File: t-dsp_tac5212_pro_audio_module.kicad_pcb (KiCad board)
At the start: 4 copper layers, 42 x 26.5 mm, 110 parts, among them J3V108 jumper, J5V108 jumper, T108 Tab, T109 Tab, T110 Tab, T111 Tab, U108 Single Buffer with Tri-state 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, U109 3.3v LDO - TLV74133PDBVR

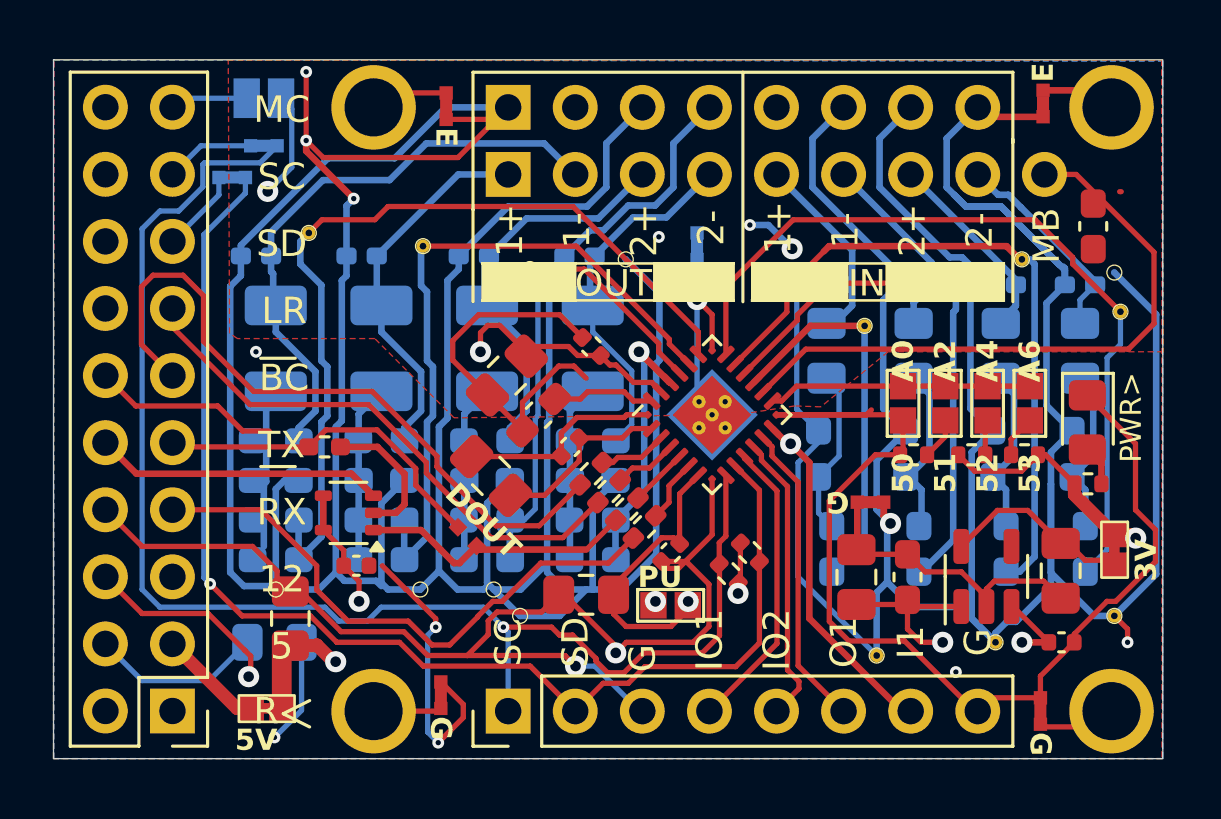
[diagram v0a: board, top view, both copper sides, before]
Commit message: Add 3D render gallery, update schematic for production
- Add interactive 3D render gallery with All Components / SMD Only tabs
- Add gallery.html page deployed to GitHub Pages alongside iBOM
- Update KiBot config: _th_ prefix file_ids, exclude_tht filter, 3d_renders_smd output
- Update CI workflow to deploy renders and gallery to GitHub Pages
- Update README with gallery thumbnail grid and links
- Schematic updates: 49.9Ω ADC input resistors, 100K bias pull-downs, component refinements
- Updated board outline footprint, schematic library, PCB layout, and 3D STEP models
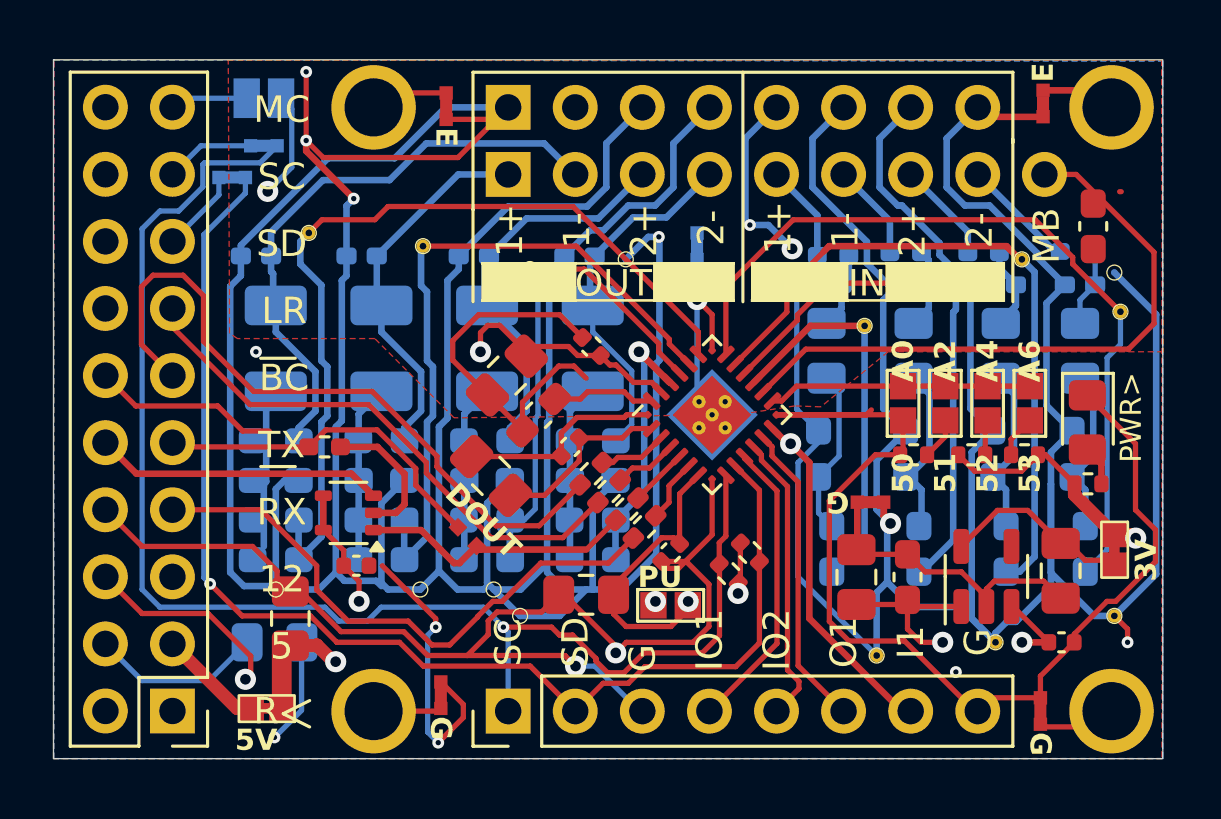
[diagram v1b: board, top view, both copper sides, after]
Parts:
- added R109: 49.9, project_fp:R_0402_1005Metric_Pad0.72x0.64mm_HandSolder, B.Cu at (120.0, 105.2)
- added R110: 49.9, project_fp:R_0402_1005Metric_Pad0.72x0.64mm_HandSolder, B.Cu at (123.5, 105.2)
- added R112: 49.9, project_fp:R_0402_1005Metric_Pad0.72x0.64mm_HandSolder, B.Cu at (117.1, 105.2)
- added R113: 49.9, project_fp:R_0402_1005Metric_Pad0.72x0.64mm_HandSolder, B.Cu at (114.3, 105.3)
- C124: value 10UF confirm polarity -> 10uF
- C125, C126, C127: value 10UF -> 10uF
- C131: footprint project_fp:C_0805_2012Metric_Pad1.15x1.40mm_HandSolder -> project_fp:C_0805_2012Metric_Pad1.18x1.45mm_HandSolder
- D108, D109, D110, D111, D112: value TPD1E10B06 -> TPD1E10B06DPYR
- D113, D114, D115: value TPD1E1B04 - 0402 size -> TPD1E10B06DPYR
- R117, R125: value 27 ohm -> 33 ohm
- TAC5212: value TAC5212 -> TAC5212IRGER
- renumbered R109 to R128, R131 to R129, R134 to R130, R136 to R134, R130 to R136, R126 to R140, R129 to R161, R116 to R162, R133 to R163
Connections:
- D112 pad 1: IN2M+ -> Net-(D112-K-Pad1)
- D113 pad 1: IN2P+ -> Net-(D113-K-Pad1)
- D114 pad 1: IN1M+ -> Net-(D114-K-Pad1)
- D115 pad 1: IN1P+ -> Net-(D115-K-Pad1)
- FB108 pad 1: IN2M+ -> Net-(D112-K-Pad1)
- FB109 pad 1: IN2P+ -> Net-(D113-K-Pad1)
- FB110 pad 1: IN1M+ -> Net-(D114-K-Pad1)
- FB111 pad 1: IN1P+ -> Net-(D115-K-Pad1)
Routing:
- net IN2P+: track 7.57 -> 3.86 mm
- net IN2M+: track 7.95 -> 4.33 mm
- net IN1M+: track 7.30 -> 3.69 mm
- net IN1P+: track 7.11 -> 3.70 mm
- net Net-(D113-K-Pad1): track 0.00 -> 3.21 mm
- net Net-(D114-K-Pad1): track 0.00 -> 3.03 mm
- net Net-(D112-K-Pad1): track 0.00 -> 3.01 mm
- net Net-(D115-K-Pad1): track 0.00 -> 2.93 mm
- net Earth: track 295.2 -> 296.4 mm

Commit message: Shrink board size to match Teensy audio adaptor shield dimensions
Update board outline width (42mm → 41.34mm), add connector 3D models
for pin sockets, and refresh PCB layout.
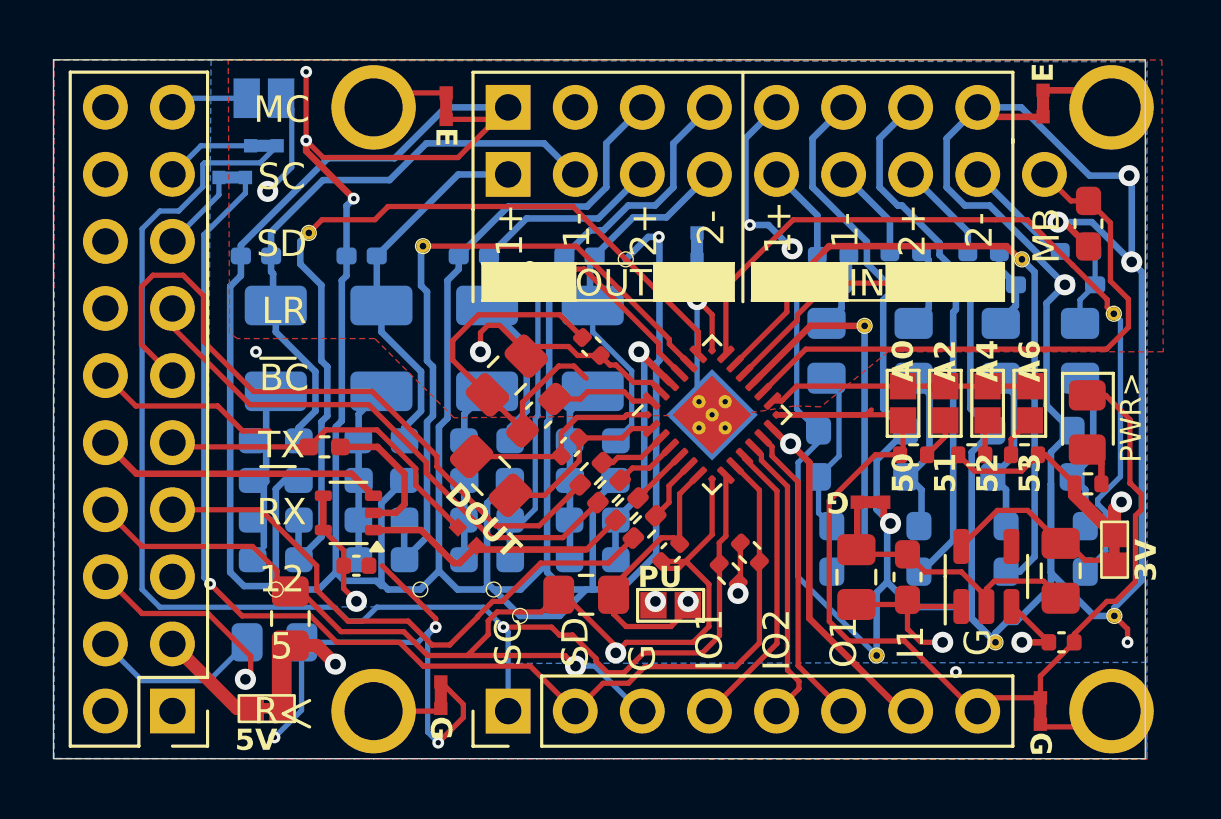
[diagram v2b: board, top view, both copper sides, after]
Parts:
- removed G108: VIA, project_fp:SMD_ROUTING_PAD
- moved T110 0.66 mm to (126.2, 103.9)
- moved T111 0.66 mm to (126.2, 118.4)
- moved INM2 0.26 mm to (125.0, 107.6)
- moved C118 0.21 mm to (124.0, 104.2)
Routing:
- net Earth: track 296.4 -> 311.3 mm, vias 9 -> 13
- net GNDD: track 170.1 -> 175.4 mm
- net MICBIAS: track 23.9 -> 22.3 mm
- added copper zone on B.Cu, net GNDD
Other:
- board size 42 x 26.5 mm -> 41.3 x 26.5 mm
